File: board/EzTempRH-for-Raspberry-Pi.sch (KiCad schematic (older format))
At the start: 13 parts, among them P1 CONN_4, P2 CONN_5, P3 CONN_5, U1 CY8C4100-28SSOP, U2 HIH5030

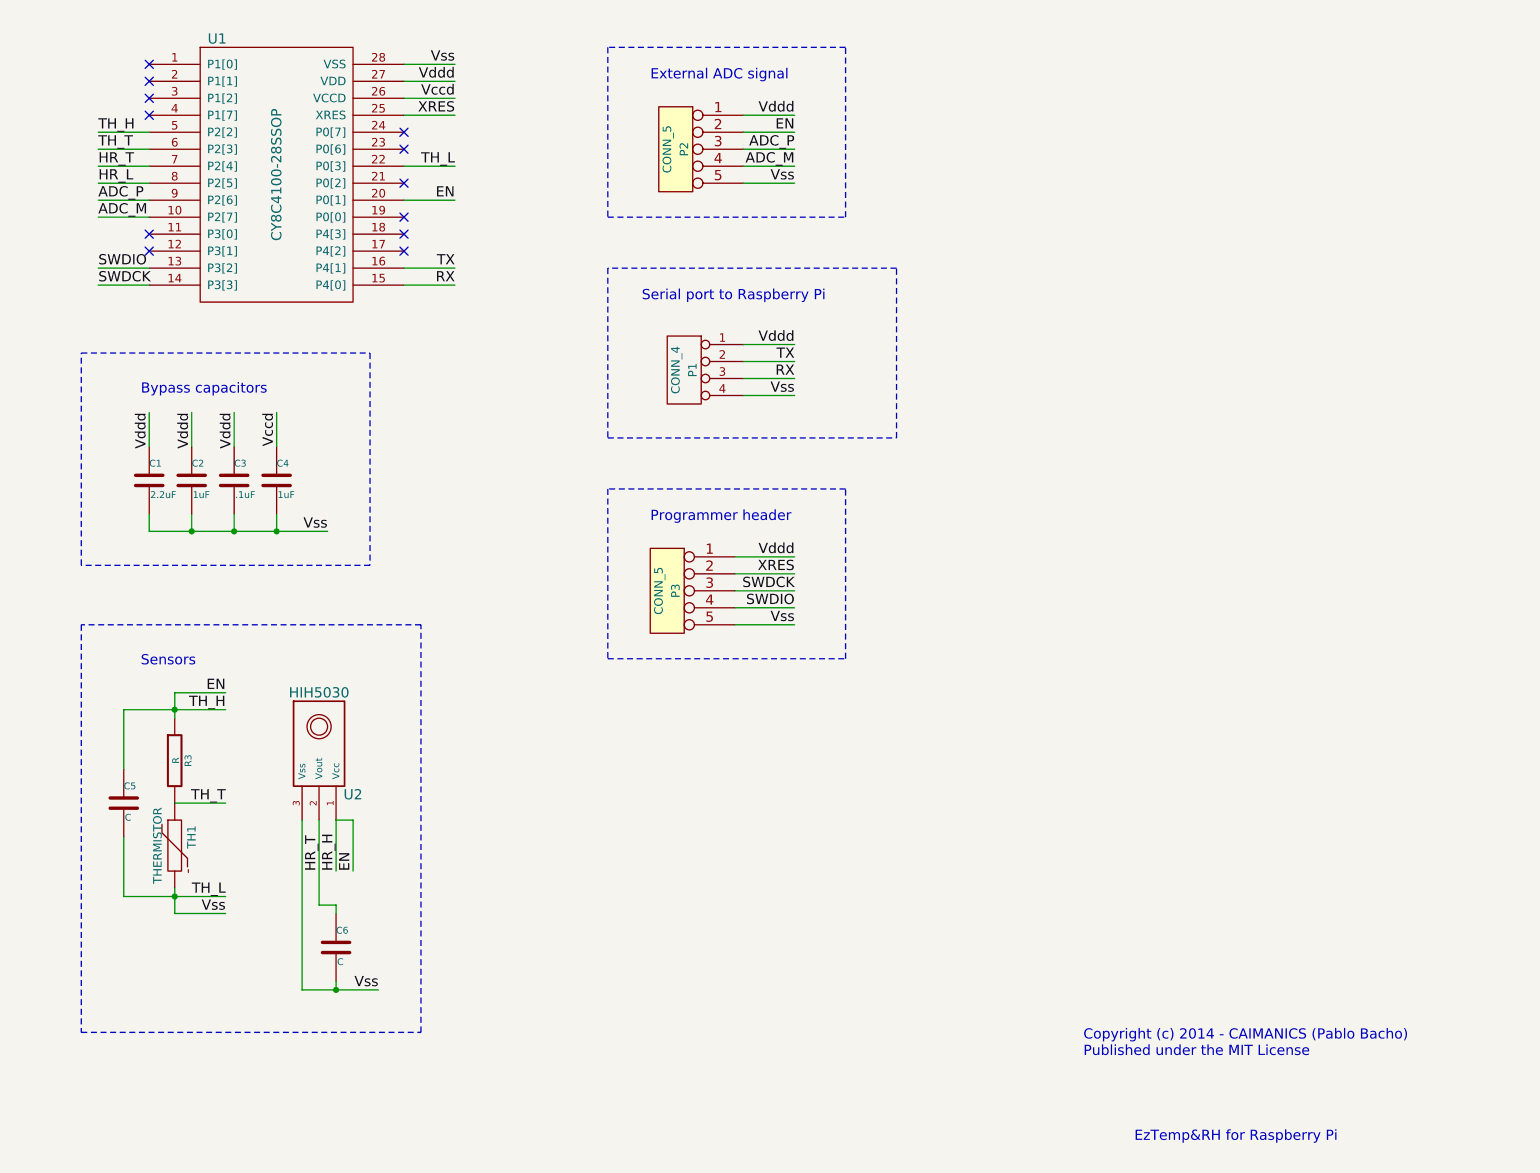
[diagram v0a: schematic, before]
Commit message: Updated schematic
- Use opamp to buffer signals.
- Added 3.3v to 1.024v voltage divider to use internal reference.
- Added voltage reading circuit
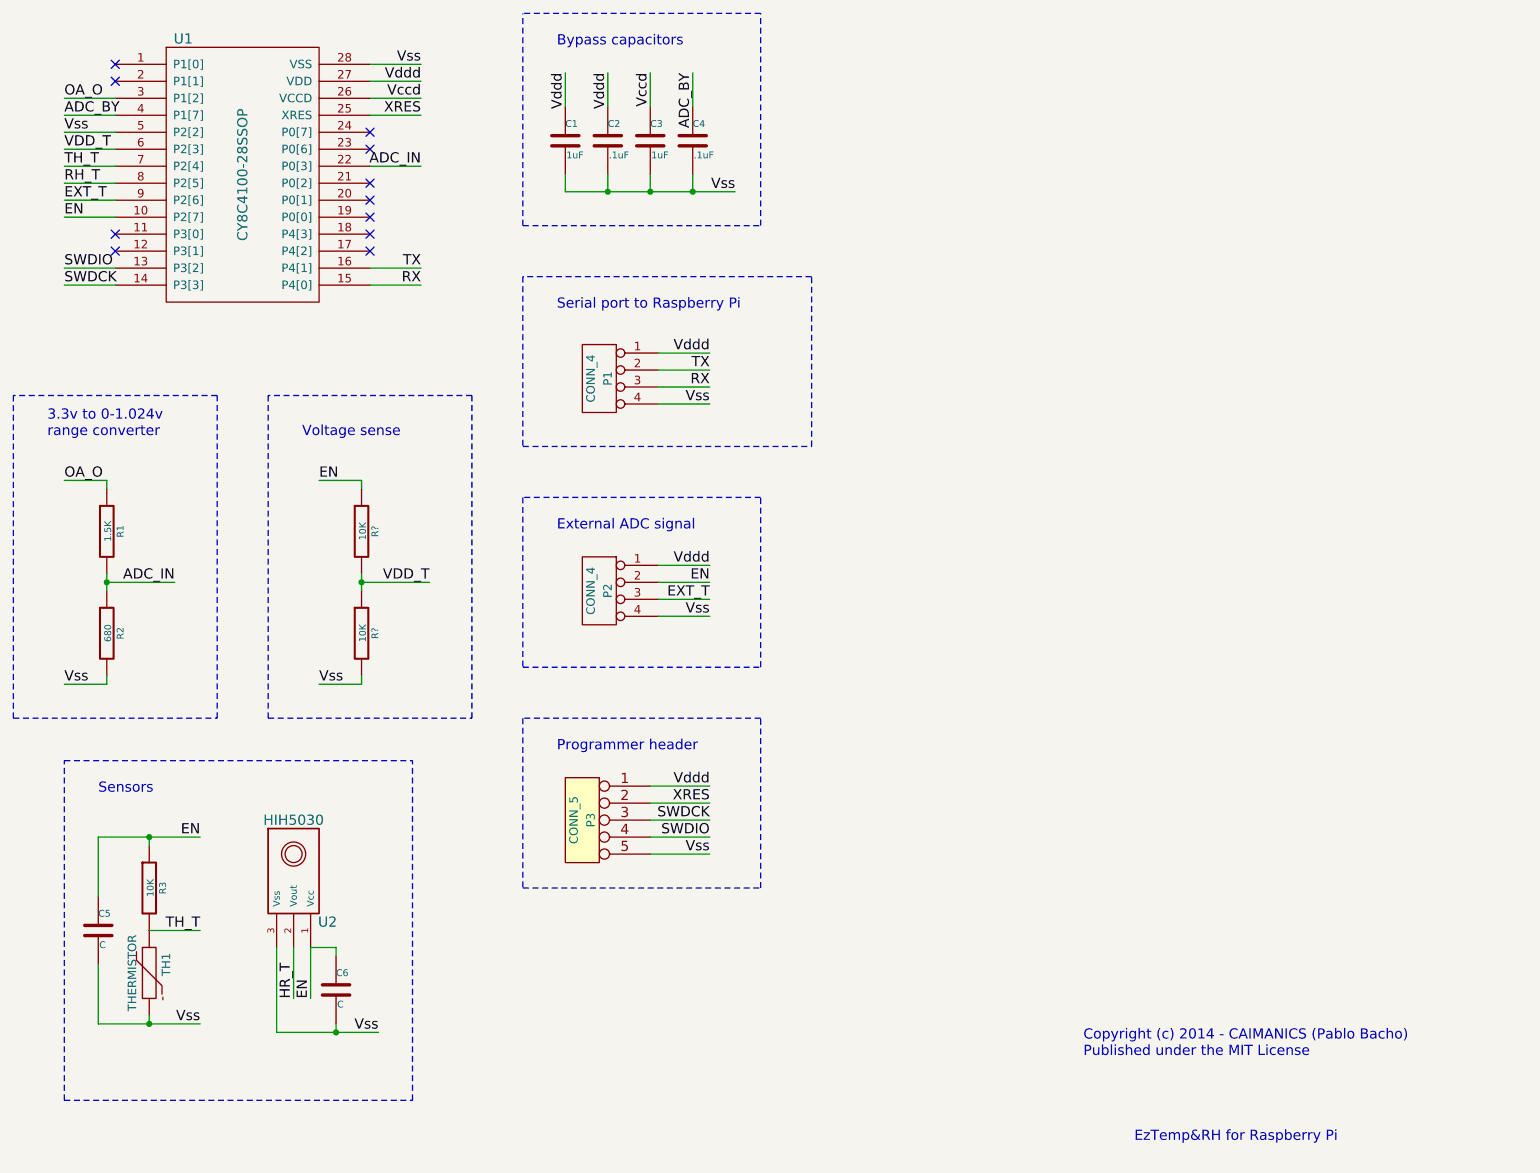
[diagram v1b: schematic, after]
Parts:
- removed P2: CONN_5, symbol CONN_5
- added P2: CONN_4, symbol CONN_4
- added R1: 1.5K, ~, symbol R
- added R2: 680, ~, symbol R
- added R? (x2): 10K, ~, symbol R
- C1: value 2.2uF -> 1uF
- C2, C4: value 1uF -> .1uF
- C3: value .1uF -> 1uF
- R3: value R -> 10K
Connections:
- net ADC_M is gone; now on net EN: U1.10 (P2[7])
- net EN: now also C6.1, P2.2 (P2), R?.1; no longer U1.20 (P0[1]), U1.5 (P2[2])
- net HR_T: no longer C6.1, U1.7 (P2[4])
- net TH_T: now also U1.7 (P2[4]); no longer U1.6 (P2[3])
- net Vccd: now also C3.1; no longer C4.1
- net Vddd: now also P2.1 (P1); no longer C3.1
- net OA_O: now reaches U1.3 (P1[2])
- net OA_O: now also R1.1
- net ADC_BY: now reaches U1.4 (P1[7])
- net ADC_BY: now also C4.1
- net ADC_P renamed EXT_T
- net EXT_T: now also P2.3 (P3)
- net HR_L renamed RH_T
- net TH_L renamed Vss
- net Vss: now also U1.5 (P2[2]), P2.4 (P4), R2.2, R?.2; no longer U1.22 (P0[3])
- new net ADC_IN: R1.2, R2.1, U1.22 (P0[3])
- new net VDD_T: R?.1, R?.2, U1.6 (P2[3])
- no-connect marks 12 -> 11
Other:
- note added: "3.3v to 0-1.024v\nrange converter"
- note added: "Voltage sense"
- moved on the sheet: C1, C2, C3, C4, C5, C6, P1, P3, R3, TH1, U1, U2

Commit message: First prototype
New schematic, now using the 1.024v reference and OpAmp buffering. Added
resistors for I2C option. First layout.
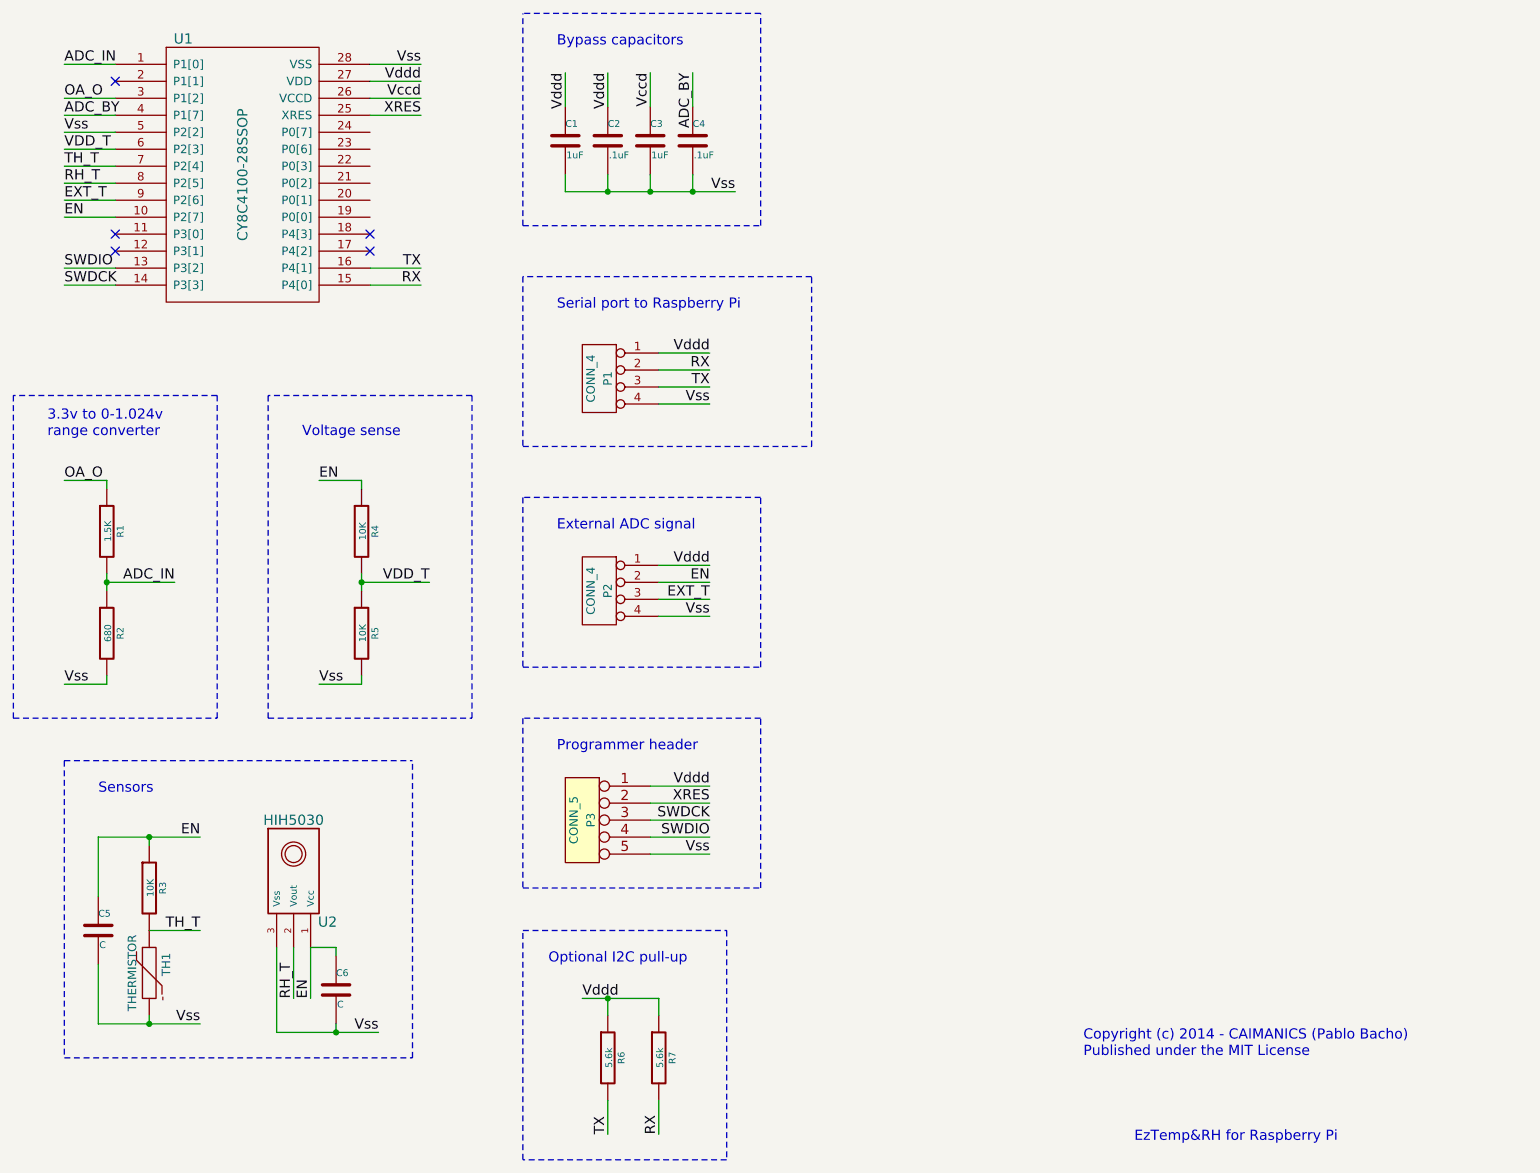
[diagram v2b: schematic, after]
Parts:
- added R6, R7: 5.6k, ~, symbol R
- gave numbers to parts that had none: 2
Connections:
- net HR_T is gone; now on net RH_T: U2.2 (Vout)
- net ADC_IN: now also U1.1 (P1[0]); no longer U1.22 (P0[3])
- net RX: now also P1.2 (P2), R7.2; no longer P1.3 (P3)
- net TX: now also P1.3 (P3), R6.2; no longer P1.2 (P2)
- net Vddd: now also R6.1, R7.1
- no-connect marks 11 -> 5
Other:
- note added: "Optional I2C pull-up"
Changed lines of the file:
@@
 Sheet 1 1
 Title ""
-Date "18 sep 2014"
+Date "23 sep 2014"
 Rev ""
 Comp ""
@@
 Text Label 3200 2500 2    60   ~ 0
 RX
-NoConn ~ 1400 1200
 NoConn ~ 1400 1300
 NoConn ~ 1400 2200
@@
 NoConn ~ 2900 2300
 NoConn ~ 2900 2200
-NoConn ~ 2900 1900
-NoConn ~ 2900 1700
-NoConn ~ 2900 1600
 Text Label 3200 1200 2    60   ~ 0
 Vss
@@
 Text Label 4900 3200 2    60   ~ 0
 Vss
+Text Label 4900 3100 2    60   ~ 0
+TX
 Text Label 4900 3000 2    60   ~ 0
-TX
-Text Label 4900 3100 2    60   ~ 0
 RX
 Text Label 4900 5450 2    60   ~ 0
@@
 Vss
 Text Label 2450 6700 1    60   ~ 0
-HR_T
+RH_T
 Text Label 2550 6700 1    60   ~ 0
 EN
-NoConn ~ 2900 2100
 Wire Wire Line
 	1100 2000 1400 2000
@@
 Wire Wire Line
 	2450 6700 2450 6400
-NoConn ~ 2900 2000
 Wire Wire Line
 	1100 1900 1400 1900
@@
 Text Label 1100 1400 0    60   ~ 0
 OA_O
-Wire Wire Line
-	3200 1800 2900 1800
-Text Label 3200 1800 2    60   ~ 0
+Text Label 1100 1200 0    60   ~ 0
 ADC_IN
 Wire Wire Line
@@
 Wire Notes Line
 	1100 5300 3150 5300
-Wire Notes Line
-	1100 7300 3150 7300
-Wire Notes Line
-	1100 7300 1100 5300
 Wire Wire Line
 	1600 5750 1600 5800
@@
 Wire Wire Line
 	2700 6400 2700 6450
-Wire Notes Line
-	3150 7300 3150 5300
 Wire Wire Line
 	1600 6850 1600 6800
@@
 	5200 900  3800 900
 $Comp
-L R R?
+L R R4
 U 1 1 541AA4FB
 P 2850 3950
-F 0 "R?" V 2930 3950 40  0000 C CNN
+F 0 "R4" V 2930 3950 40  0000 C CNN
 F 1 "10K" V 2857 3951 40  0000 C CNN
 F 2 "~" V 2780 3950 30  0000 C CNN
@@
 $EndComp
 $Comp
-L R R?
+L R R5
 U 1 1 541AA501
 P 2850 4550
-F 0 "R?" V 2930 4550 40  0000 C CNN
+F 0 "R5" V 2930 4550 40  0000 C CNN
 F 1 "10K" V 2857 4551 40  0000 C CNN
 F 2 "~" V 2780 4550 30  0000 C CNN
@@
 Wire Notes Line
 	3500 3150 2300 3150
+Wire Notes Line
+	1100 5300 1100 7050
+Wire Notes Line
+	1100 7050 3150 7050
+Wire Notes Line
+	3150 7050 3150 5300
+Wire Wire Line
+	1100 1200 1400 1200
+$Comp
+L R R6
+U 1 1 542174F8
+P 4300 7050
+F 0 "R6" V 4380 7050 40  0000 C CNN
+F 1 "5.6k" V 4307 7051 40  0000 C CNN
+F 2 "~" V 4230 7050 30  0000 C CNN
+F 3 "~" H 4300 7050 30  0000 C CNN
+	1    4300 7050
+	1    0    0    -1
+$EndComp
+$Comp
+L R R7
+U 1 1 54217507
+P 4600 7050
+F 0 "R7" V 4680 7050 40  0000 C CNN
+F 1 "5.6k" V 4607 7051 40  0000 C CNN
+F 2 "~" V 4530 7050 30  0000 C CNN
+F 3 "~" H 4600 7050 30  0000 C CNN
+	1    4600 7050
+	1    0    0    -1
+$EndComp
+Wire Wire Line
+	4600 6700 4600 6800
+Wire Wire Line
+	4150 6700 4600 6700
+Wire Wire Line
+	4300 6700 4300 6800
+Connection ~ 4300 6700
+Wire Wire Line
+	4300 7300 4300 7500
+Wire Wire Line
+	4600 7300 4600 7500
+Text Label 4150 6700 0    60   ~ 0
+Vddd
+Text Label 4300 7500 1    60   ~ 0
+TX
+Text Label 4600 7500 1    60   ~ 0
+RX
+Text Notes 3950 6500 0    60   ~ 0
+Optional I2C pull-up
+Wire Notes Line
+	3800 6300 5000 6300
+Wire Notes Line
+	5000 6300 5000 7650
+Wire Notes Line
+	5000 7650 3800 7650
+Wire Notes Line
+	3800 7650 3800 6300
 $EndSCHEMATC
